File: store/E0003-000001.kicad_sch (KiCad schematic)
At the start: 18 parts, among them J8 Seansor_Header_A, J9 Seansor_Header_B, U1 AS7343-DLGM, U2 AS7331-AQFM, U3 TLV70018

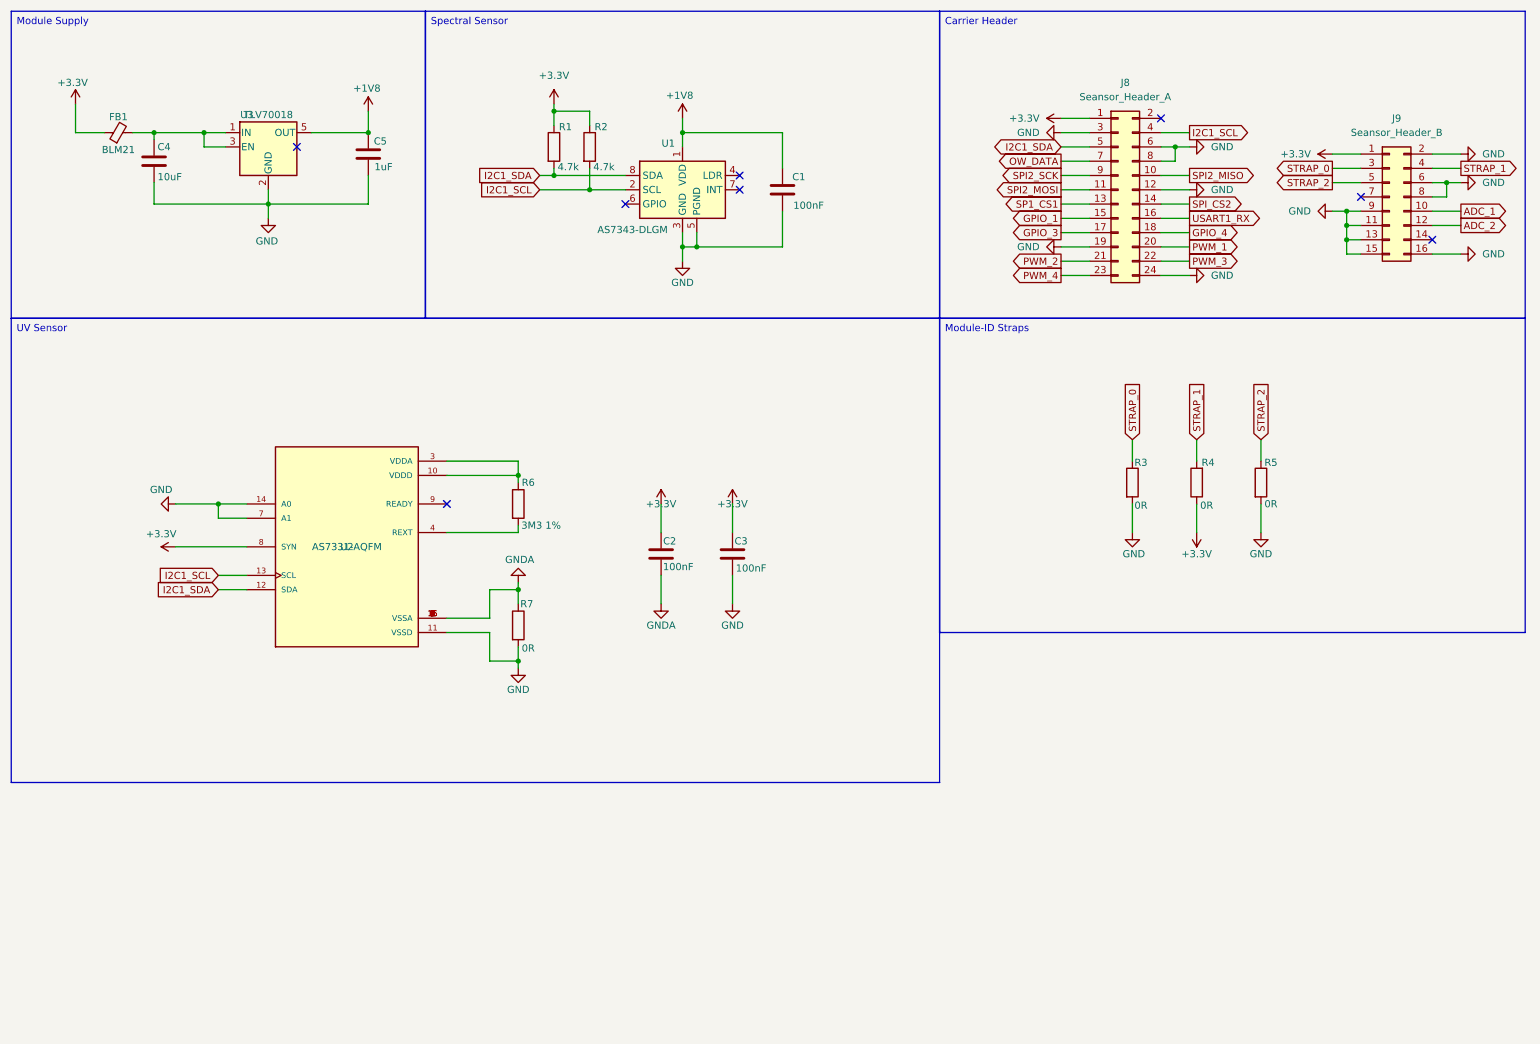
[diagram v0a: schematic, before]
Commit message: store: fit the PCA9306 level translator on E0003
store/E0003-000001.kicad_sch: add U4 PCA9306 with R8/R9 4.7 k pull-ups to
3.3 V, R10 200 k on EN and C6 on VREF2; retie R1/R2 to +1V8 and rename
U1's segment to I2C1_SCL_1V8 / I2C1_SDA_1V8.
spec/M02-LIGHT-specification.md: add U4 to §4.2, split the pull-ups over
two segments in §5.1, state U4's requirements in §5.2, restate the 1.8 V
rail load in §7.3, rewrite V5 against the 1.8 V sub-segment, close O-56
and add U4's ordering code to O-62.

Signed-off-by: IIchukissII <133657307+IIchukissII@users.noreply.github.com>
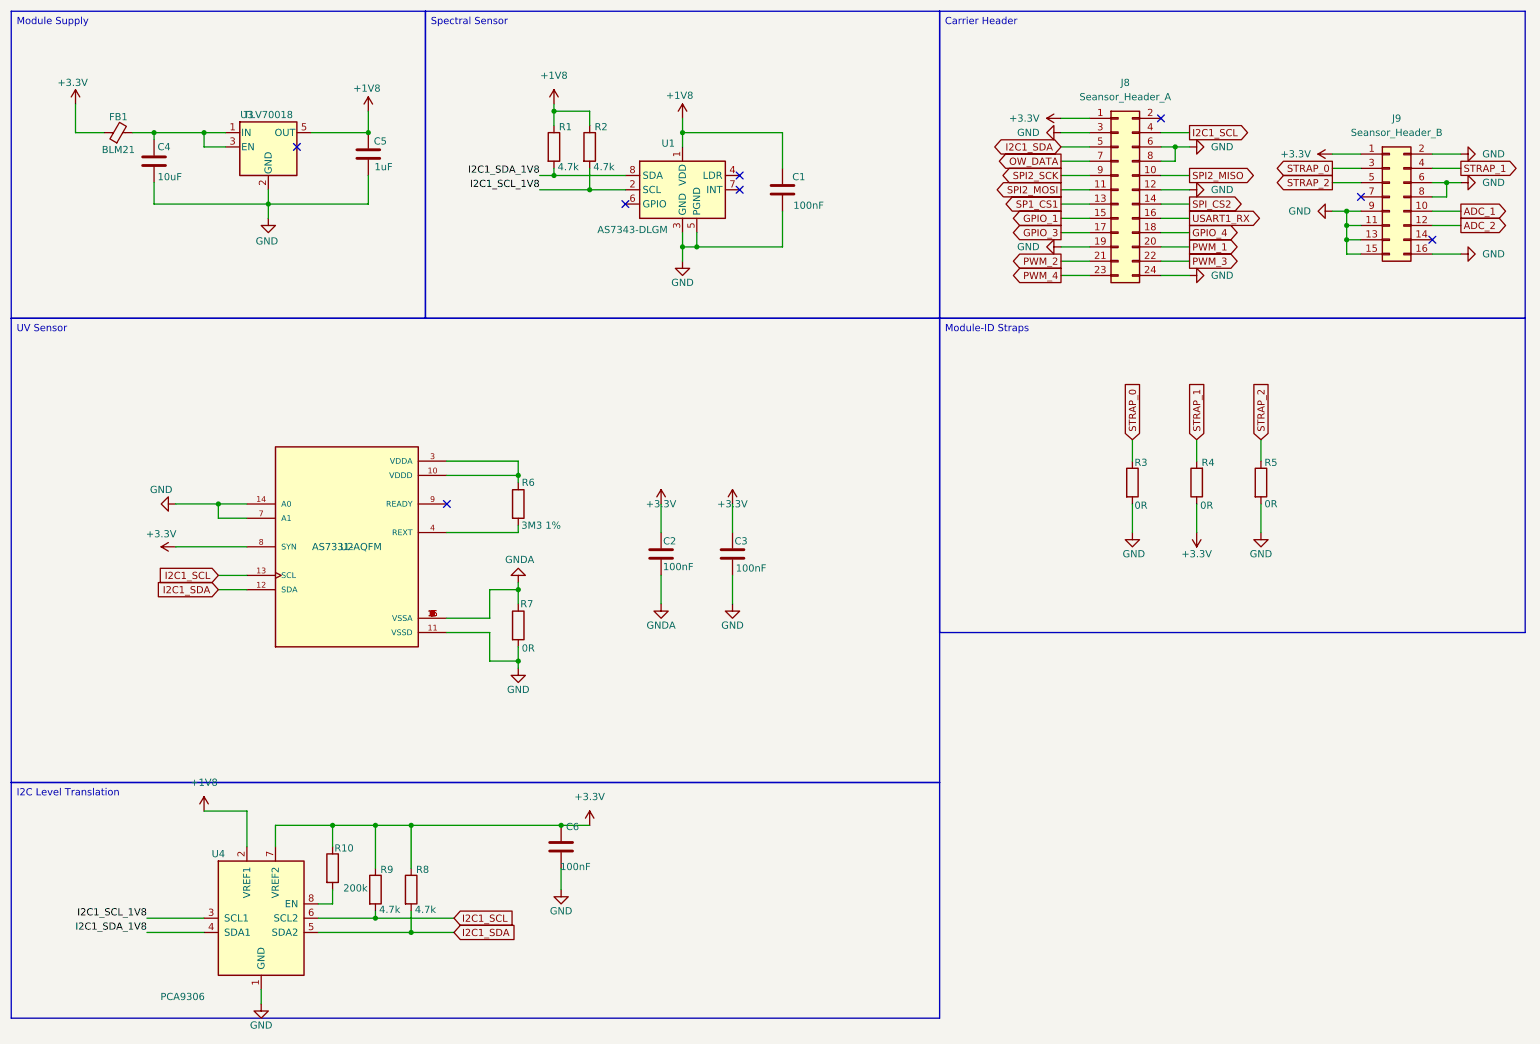
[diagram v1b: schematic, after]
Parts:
- added C6: 100nF, Capacitor_SMD:C_0805_2012Metric, symbol Device:C
- added R10: 200k, Resistor_SMD:R_0805_2012Metric, symbol Device:R
- added R8, R9: 4.7k, Resistor_SMD:R_0805_2012Metric, symbol Device:R
- added U4: PCA9306, Package_SO:VSSOP-8_2.3x2mm_P0.5mm, symbol Interface:PCA9306
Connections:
- net +1V8: now also R1.1, R2.1, U4.2 (VREF1)
- net +3.3V: now also C6.1, R10.1, R8.1, R9.1, U4.7 (VREF2); no longer R1.1, R2.1
- net GND: now also C6.2, U4.1 (GND)
- net I2C1_SCL: now also R9.2, U4.6 (SCL2); no longer R2.2, U1.2 (SCL)
- net I2C1_SDA: now also R8.2, U4.5 (SDA2); no longer R1.2, U1.8 (SDA)
- new net: R10.2, U4.8 (EN)
- new net I2C1_SCL_1V8: R2.2, U1.2 (SCL), U4.3 (SCL1)
- new net I2C1_SDA_1V8: R1.2, U1.8 (SDA), U4.4 (SDA1)
